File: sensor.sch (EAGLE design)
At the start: 27 parts, among them U1 NX1117C33Z, U2 NX1117CE50Z, U3 BMP180, U4 TSL2561

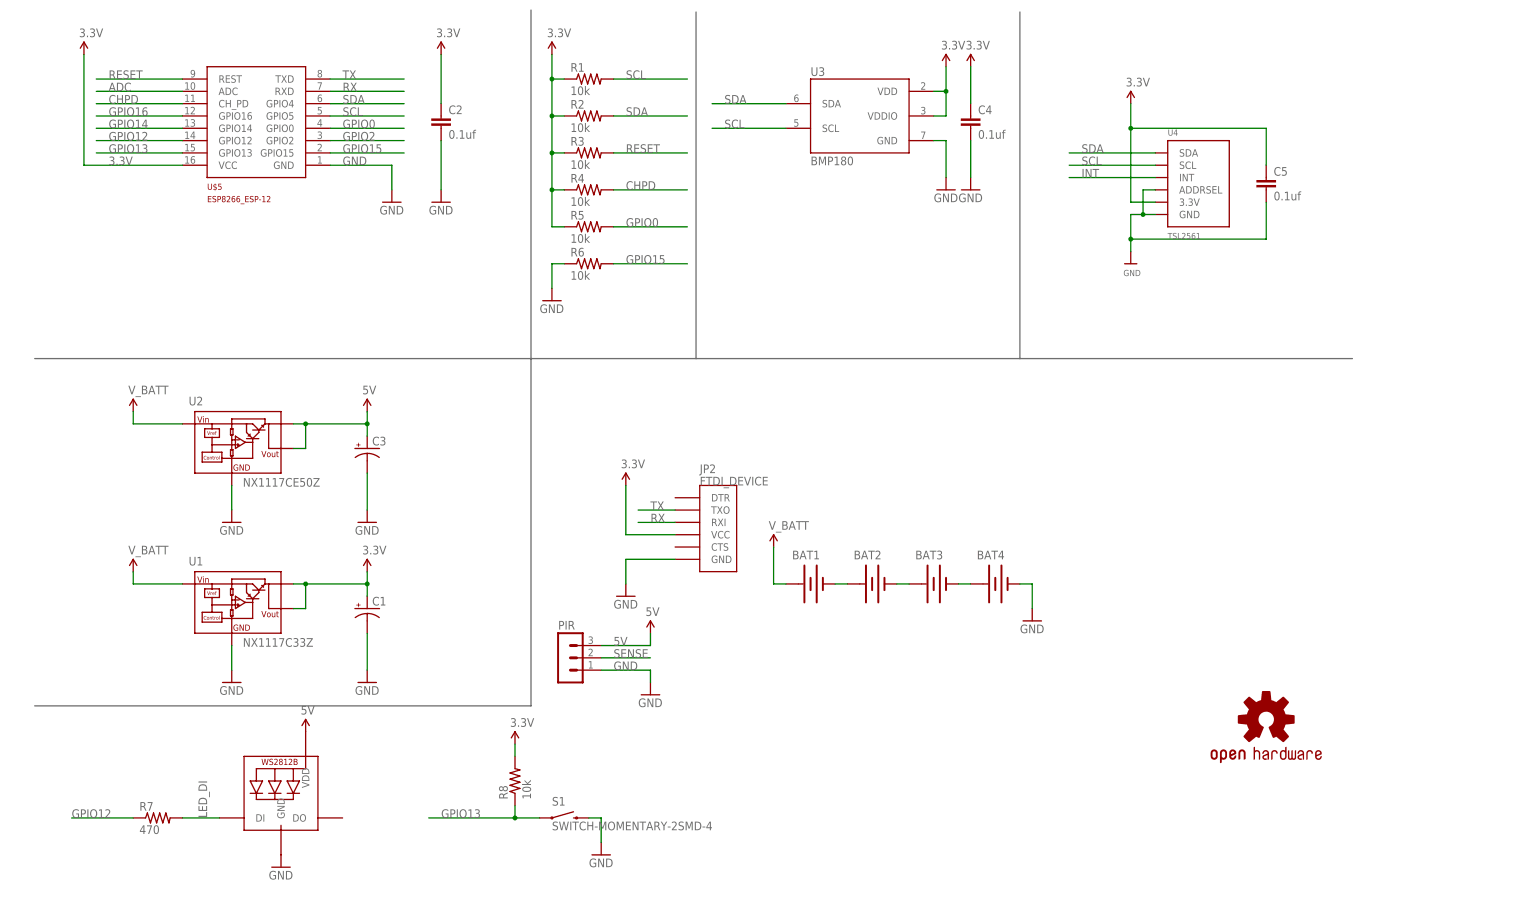
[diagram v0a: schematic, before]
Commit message: lipo 18650 cell, TP4056 1A boost/charge controller
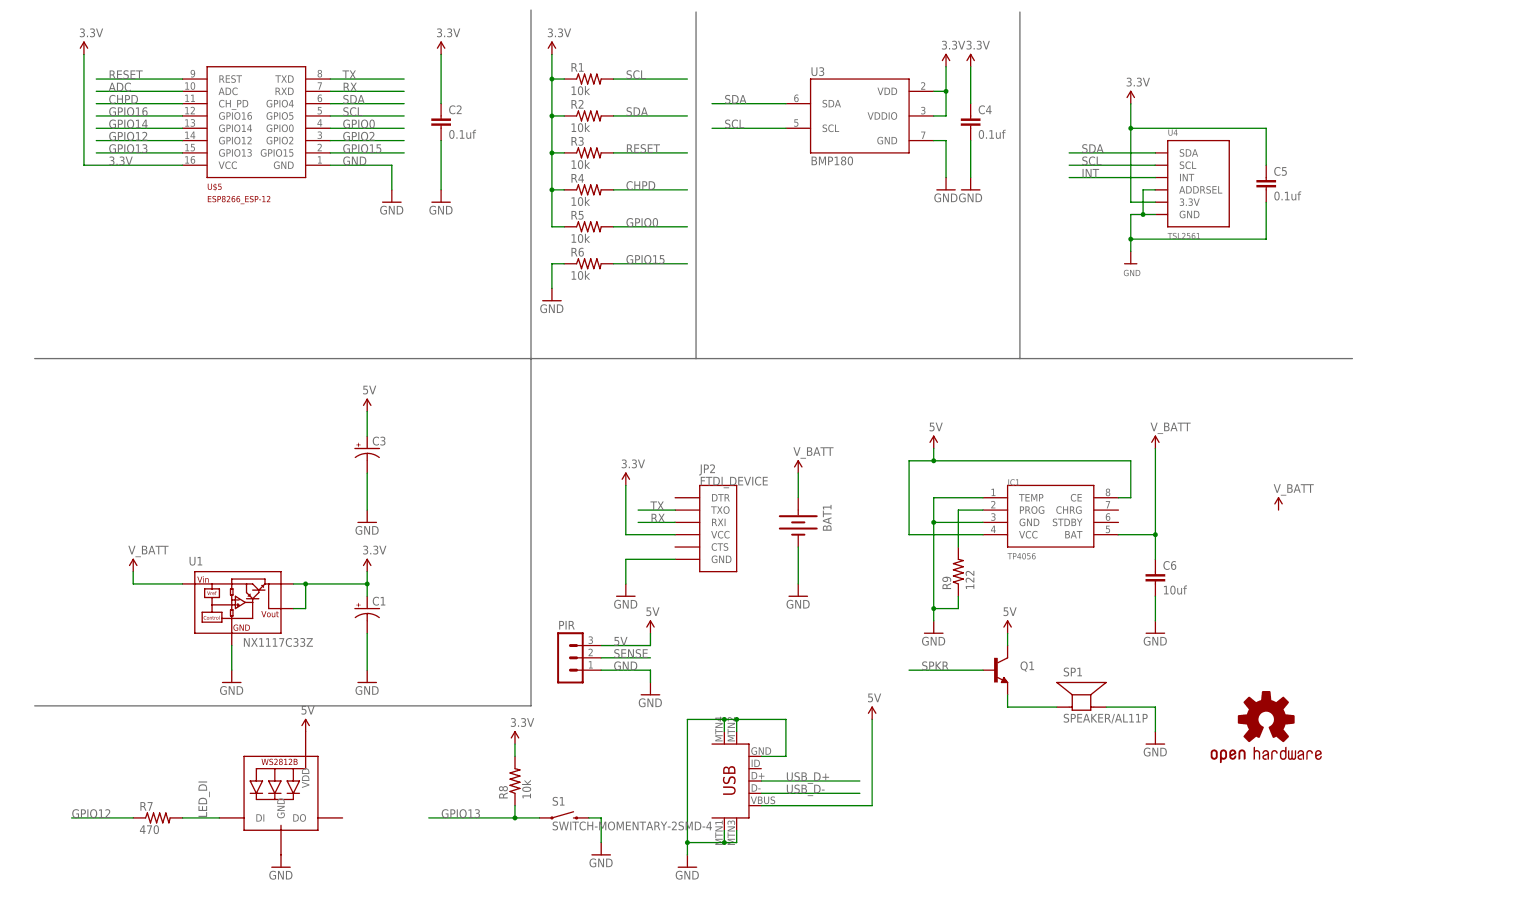
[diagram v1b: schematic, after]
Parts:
- removed BAT2, BAT3, BAT4: (no value), SparkFun-Electromechanical:BATTERYAA
- removed U2: NX1117CE50Z, nxp_60:NX1117CE50Z
- added C6: 10uf, SparkFun-Capacitors:CAP0805
- added IC1: TP4056, TP4056:TP4056
- added Q1: (no value), SparkFun-DiscreteSemi:TRANSISTOR_NPNSOT23-3
- added R9: 122, SparkFun-Resistors:RESISTOR0805-RES
- added SP1: SPEAKER/AL11P, adafruit:SPEAKER/AL11P
- added U$6: USB-MINIB-5PIN, SparkFun-Connectors:USB-MINIB-5PIN
- BAT1: device SparkFun-Electromechanical:BATTERYAA -> SparkFun-Electromechanical:BATTERY18650
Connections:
- removed net N$1: BAT1.-, BAT2.+
- new net N$6: Q1.E, SP1.+
- new net SPKR: Q1.B
- new net USB_D+: U$6.D+
- new net USB_D-: U$6.D-
- net 5V: now also IC1.CE, IC1.VCC, Q1.C, U$6.VBUS; no longer U2.VOUT, U2.VOUT1
- net GND: now also BAT1.-, C6.2, SP1.-, U$6.GND, U$6.MTN1, U$6.MTN2, U$6.MTN3, U$6.MTN4; no longer BAT4.-, U2.GND
- net N$2: now also IC1.GND, IC1.TEMP, R9.1; no longer BAT2.-, BAT3.+
- net N$3: now also IC1.PROG, R9.2; no longer BAT3.-, BAT4.+
- net V_BATT: now also C6.1, IC1.BAT; no longer U2.VIN
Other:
- moved on the sheet: BAT1

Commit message: Move schematic around to be more pleasing, add i2c header as per @badspyro's request.
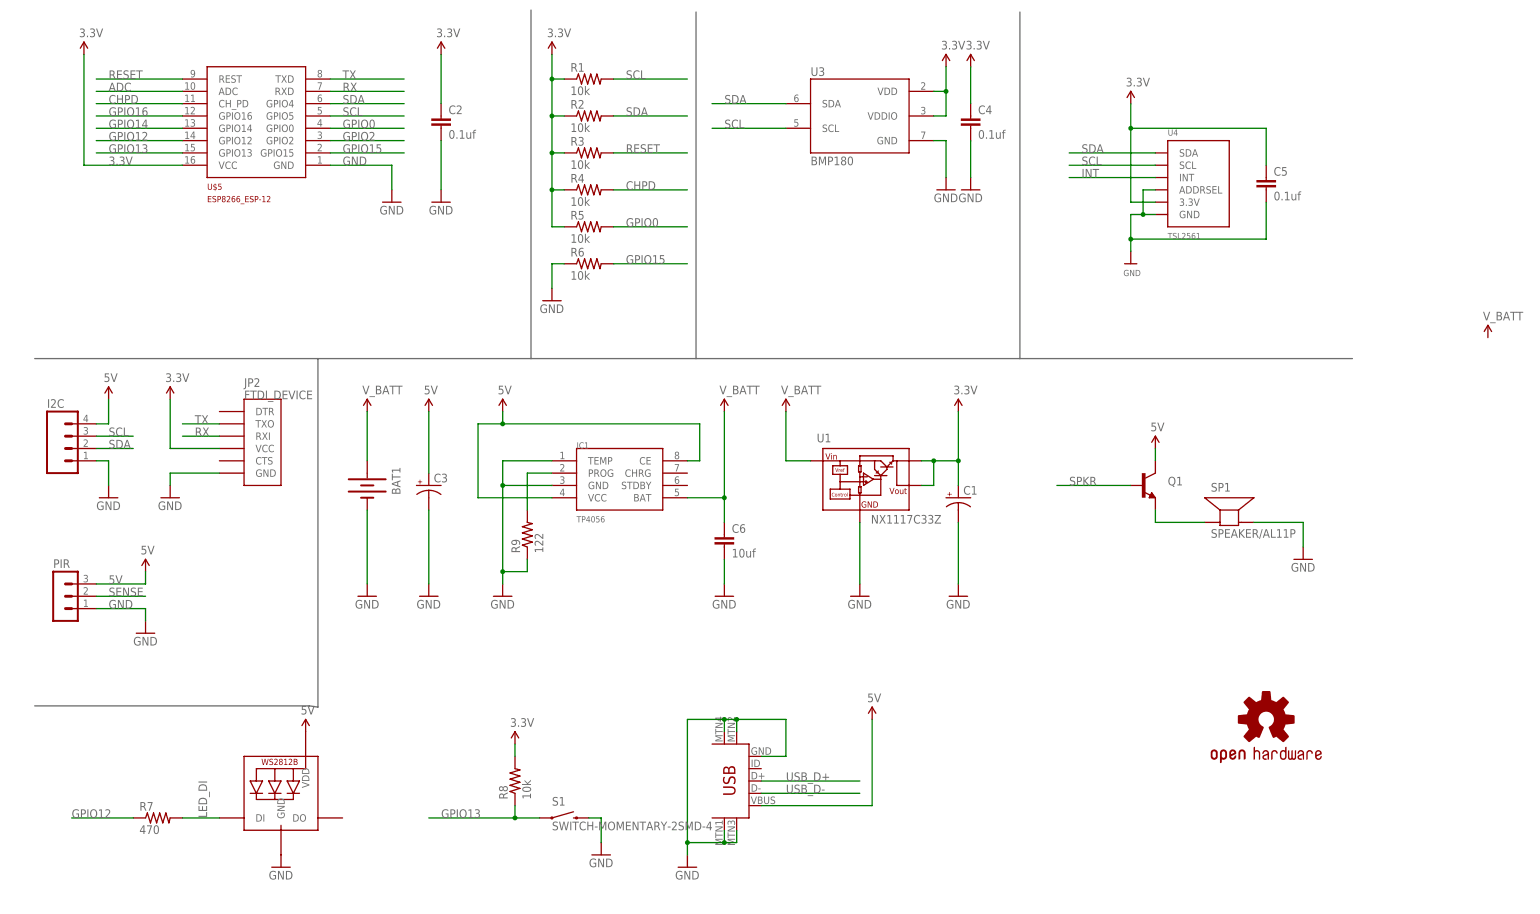
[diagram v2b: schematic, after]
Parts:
- added I2C: (no value), SparkFun-Connectors:M04JST-PTH
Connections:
- net 5V: now also I2C.4
- net GND: now also I2C.1
- net SCL: now also I2C.3
- net SDA: now also I2C.2
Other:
- moved on the sheet: BAT1, C1, C3, C6, IC1, JP2, PIR, Q1, R9, SP1, U1

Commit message: Redo.. but oops.
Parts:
- removed C3: (no value), SparkFun-Capacitors:47UF-50V-20%(ELECT)
- removed LED1: WS2812B3535, adafruit:WS2812B3535
- removed R7: 470, SparkFun-Resistors:RESISTOR0805-RES
- removed R8: 10k, SparkFun-Resistors:RESISTOR0805-RES
- added C7: 0.1uF, rcl:C-EUC0805
- added C8, C9: 22pf, rcl:C-EUC0805
- added LED2: LED-TRICOLOR-5050NO_IC, SparkFun-LED:LED-TRICOLOR-5050NO_IC
- added U$11: CH340G, CH340G-USB-SERIAL:CH340G
- added Y1: 12mhz, SparkFun-FreqCtrl:CRYSTALSMD
- C6: value 10uf -> (none); device SparkFun-Capacitors:CAP0805 -> SparkFun-Capacitors:47UF-50V-20%(ELECT)
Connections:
- removed net LED_DI: LED1.DI, R7.2
- removed net N$2: IC1.GND, IC1.TEMP, R9.1
- removed net SENSE: PIR.2
- removed net SPKR: Q1.B
- new net OSCI: C8.1, U$11.XI, Y1.1
- new net OSCO: C9.1, U$11.XO, Y1.2
- net 3.3V: now also C7.1, I2C.4, PIR.3, Q1.C, U$11.V3, U$11.VCC; no longer R8.2
- net 5V: no longer C3.+, I2C.4, LED1.VDD, PIR.3, Q1.C
- net GND: now also C6.-, C7.2, C8.2, C9.2, IC1.GND, IC1.TEMP, LED2.BLU-C, LED2.GRN-C, LED2.RED-C, R9.1, U$11.GND; no longer C3.-, C6.2, LED1.GND
- net GPIO0: now also S1.1
- net GPIO12: now also LED2.BLU-A; no longer R7.1
- net GPIO13: now also Q1.B; no longer R8.1, S1.1
- net GPIO14: now also LED2.RED-A
- net GPIO16: now also LED2.GRN-A
- net GPIO2: now also PIR.2
- net RX: now also U$11.TX
- net TX: now also U$11.RX
- net USB_D+: now also U$11.D+
- net USB_D-: now also U$11.D-
- net V_BATT: now also C6.+; no longer C6.1

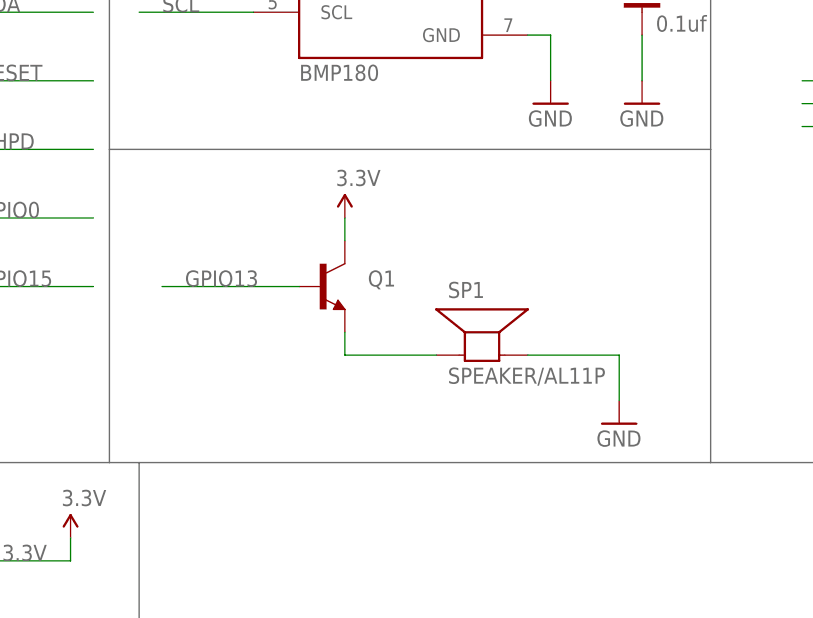
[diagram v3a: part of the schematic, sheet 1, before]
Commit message: Redone this time without the esp8266's housing clipping through the PIR variable resistors
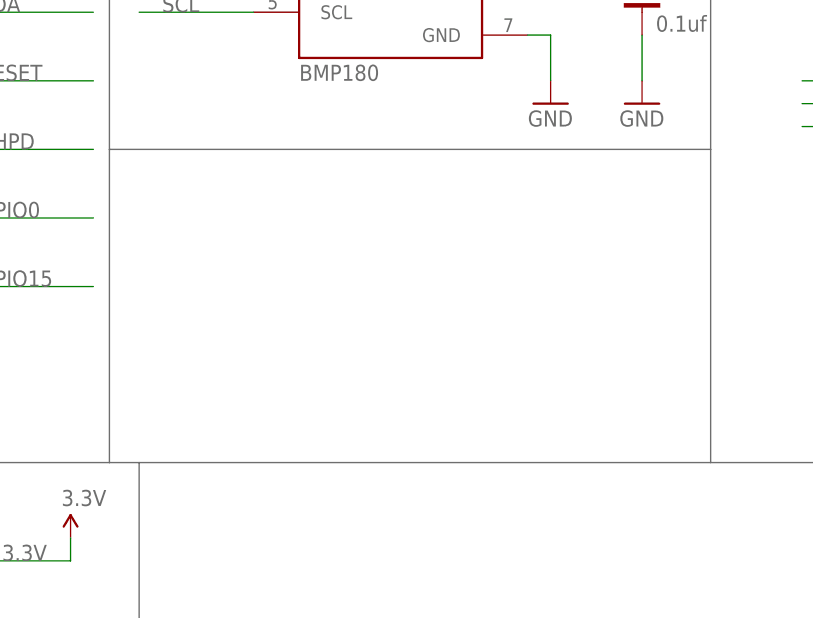
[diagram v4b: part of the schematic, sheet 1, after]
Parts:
- removed Q1: (no value), SparkFun-DiscreteSemi:TRANSISTOR_NPNSOT23-3
- removed SP1: SPEAKER/AL11P, adafruit:SPEAKER/AL11P
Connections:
- removed net N$6: Q1.E, SP1.+
- net 3.3V: no longer Q1.C
- net GND: no longer SP1.-
- net GPIO13: no longer Q1.B
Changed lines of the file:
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@@
 <part name="GND16" library="SparkFun" deviceset="GND" device=""/>
 <part name="R9" library="SparkFun-Resistors" deviceset="RESISTOR" device="0805-RES" value="122"/>
-<part name="SP1" library="adafruit" deviceset="SPEAKER" device="/AL11P"/>
-<part name="GND17" library="SparkFun" deviceset="GND" device=""/>
-<part name="Q1" library="SparkFun-DiscreteSemi" deviceset="TRANSISTOR_NPN" device="SOT23-3"/>
 <part name="I2C" library="SparkFun-Connectors" deviceset="M04" device="JST-PTH"/>
 <part name="GND18" library="SparkFun" deviceset="GND" device=""/>
@@
 <part name="GND1" library="SparkFun" deviceset="GND" device=""/>
 <part name="FRAME1" library="SparkFun-Aesthetics" deviceset="FRAME-A4L" device=""/>
-<part name="SUPPLY18" library="SparkFun-Aesthetics" deviceset="3.3V" device=""/>
 </parts>
 <sheets>
@@
 <instance part="SUPPLY10" gate="G$1" x="226.06" y="160.02"/>
 <instance part="C5" gate="G$1" x="254" y="142.24"/>
-<instance part="SP1" gate="S1" x="177.8" y="119.38"/>
-<instance part="GND17" gate="1" x="193.04" y="111.76"/>
-<instance part="Q1" gate="G$1" x="160.02" y="127"/>
 <instance part="I2C" gate="G$1" x="7.62" y="88.9"/>
 <instance part="GND18" gate="1" x="15.24" y="78.74"/>
@@
 <instance part="GND1" gate="1" x="63.5" y="12.7"/>
 <instance part="FRAME1" gate="G$1" x="0" y="0"/>
-<instance part="SUPPLY18" gate="G$1" x="162.56" y="134.62"/>
 </instances>
 <busses>
@@
 <pinref part="SUPPLY17" gate="G$1" pin="3.3V"/>
 </segment>
-<segment>
-<pinref part="Q1" gate="G$1" pin="C"/>
-<wire x1="162.56" y1="134.62" x2="162.56" y2="132.08" width="0.1524" layer="91"/>
-<pinref part="SUPPLY18" gate="G$1" pin="3.3V"/>
-</segment>
 </net>
 <net name="GND" class="0">
@@
 </segment>
 <segment>
-<pinref part="SP1" gate="S1" pin="-"/>
-<pinref part="GND17" gate="1" pin="GND"/>
-<wire x1="182.88" y1="119.38" x2="193.04" y2="119.38" width="0.1524" layer="91"/>
-<wire x1="193.04" y1="119.38" x2="193.04" y2="114.3" width="0.1524" layer="91"/>
-</segment>
-<segment>
 <pinref part="I2C" gate="G$1" pin="1"/>
 <wire x1="12.7" y1="86.36" x2="15.24" y2="86.36" width="0.1524" layer="91"/>
@@
 <label x="15.24" y="149.86" size="1.778" layer="95"/>
 </segment>
-<segment>
-<pinref part="Q1" gate="G$1" pin="B"/>
-<wire x1="157.48" y1="127" x2="142.24" y2="127" width="0.1524" layer="91"/>
-<label x="144.78" y="127" size="1.778" layer="95"/>
-</segment>
 </net>
 <net name="GPIO12" class="0">
@@
 </segment>
 </net>
-<net name="N$6" class="0">
-<segment>
-<pinref part="Q1" gate="G$1" pin="E"/>
-<wire x1="162.56" y1="121.92" x2="162.56" y2="119.38" width="0.1524" layer="91"/>
-<pinref part="SP1" gate="S1" pin="+"/>
-<wire x1="162.56" y1="119.38" x2="172.72" y2="119.38" width="0.1524" layer="91"/>
-</segment>
-</net>
